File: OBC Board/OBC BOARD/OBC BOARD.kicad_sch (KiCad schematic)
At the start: 0 parts

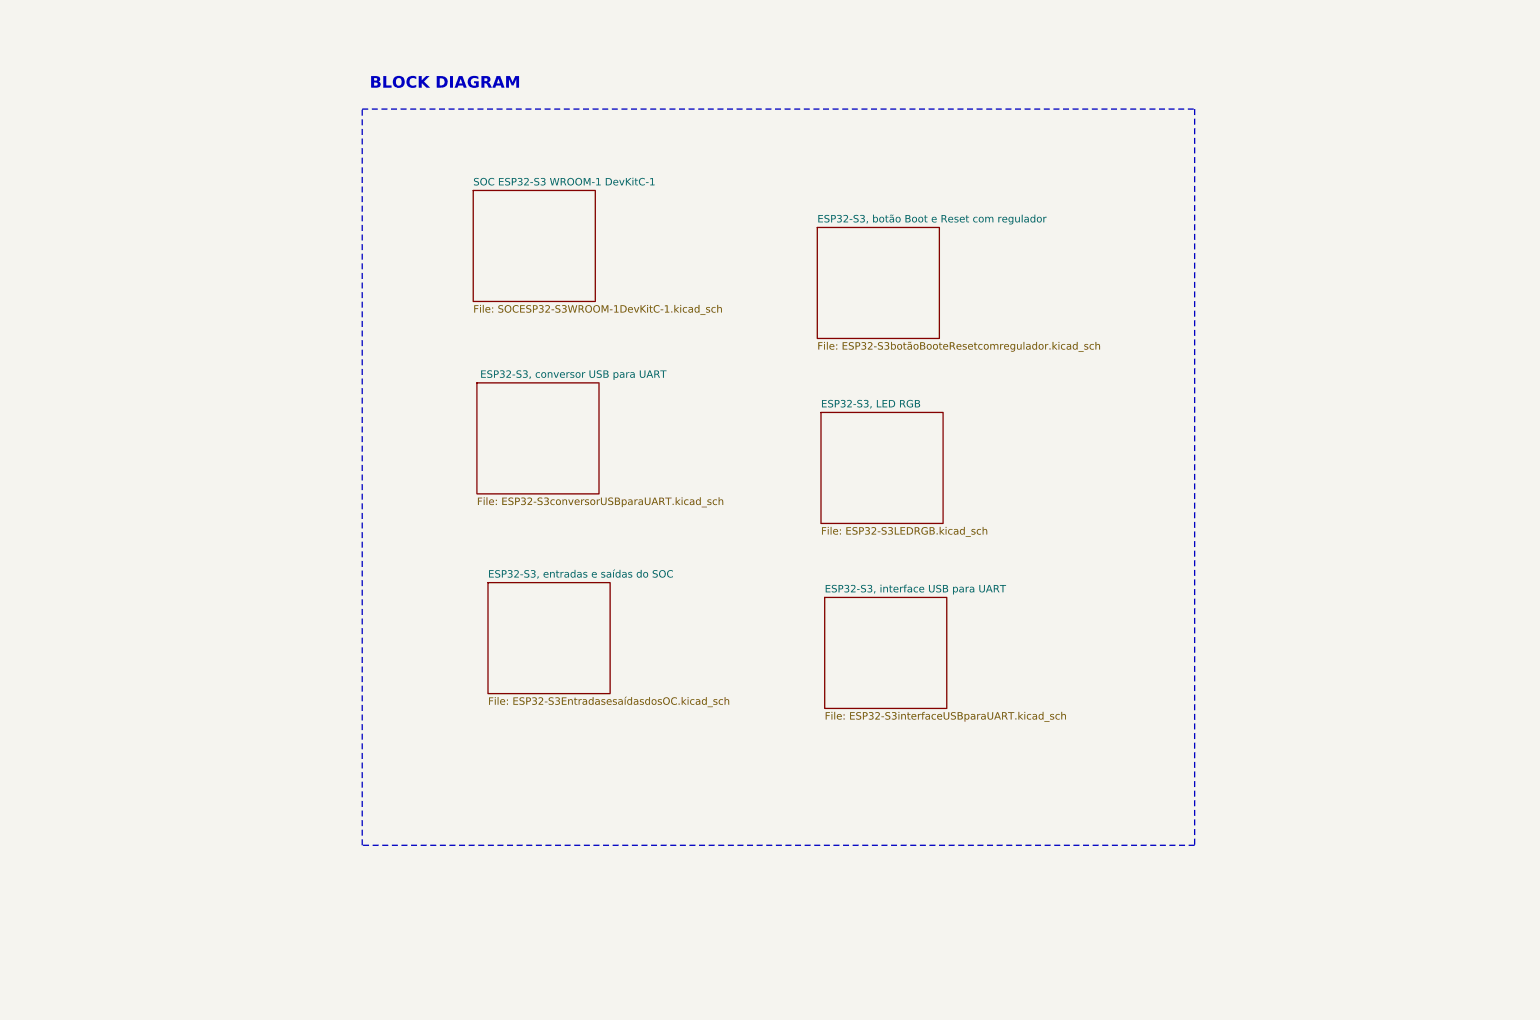
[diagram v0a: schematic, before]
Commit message: Realização do diagrama de blocos, test points, padronização e mudança dos caminhos das bibliotecas de footprints e simbolos
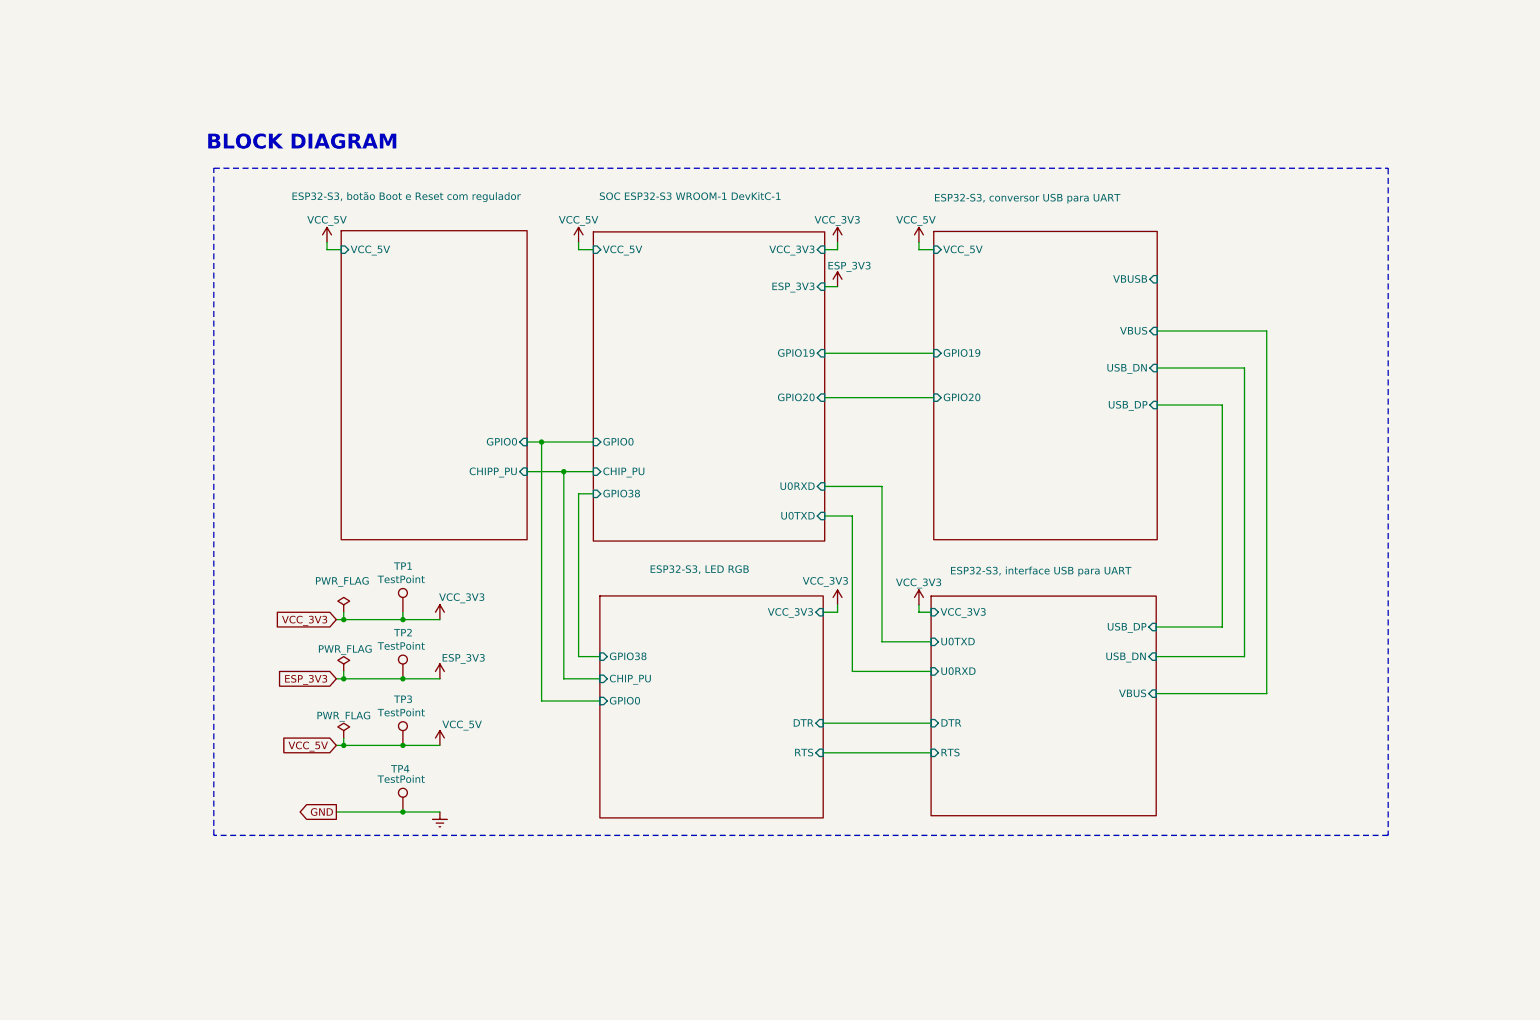
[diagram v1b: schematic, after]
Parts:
- added TP1, TP2, TP3, TP4: TestPoint, TestPoint:TestPoint_Pad_4.0x4.0mm, symbol Connector:TestPoint
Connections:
- new net ESP_3V3: TP2.1
- new net Earth: TP4.1
- new net VCC_3V3: TP1.1
- new net VCC_5V: TP3.1
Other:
- removed sheet ESP32-S3, entradas e saídas do SOC
- sheet  ESP32-S3, conversor USB para UART ports: added GPIO19, GPIO20, USB_DN, USB_DP, VBUS, VBUSB, VCC_5V; removed none
- sheet ESP32-S3, LED RGB ports: added CHIP_PU, DTR, GPIO0, GPIO38, RTS, VCC_3V3; removed none
- sheet ESP32-S3, botão Boot e Reset com regulador ports: added CHIPP_PU, GPIO0, VCC_5V; removed none
- sheet ESP32-S3, interface USB para UART ports: added DTR, RTS, U0RXD, U0TXD, USB_DN, USB_DP, VBUS, VCC_3V3; removed none
- sheet SOC ESP32-S3 WROOM-1 DevKitC-1 ports: added CHIP_PU, ESP_3V3, GPIO0, GPIO19, GPIO20, GPIO38, U0RXD, U0TXD, VCC_3V3, VCC_5V; removed none
- title: ICARUS-2 OBCH -> ICARUS-2 OBDH

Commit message: Junção dos projetos FPGA e ESP32. Biblioteca de simbolos e footprints realizadas. Definição do caminho para os arquivos. Inclusão do esquema librecube.
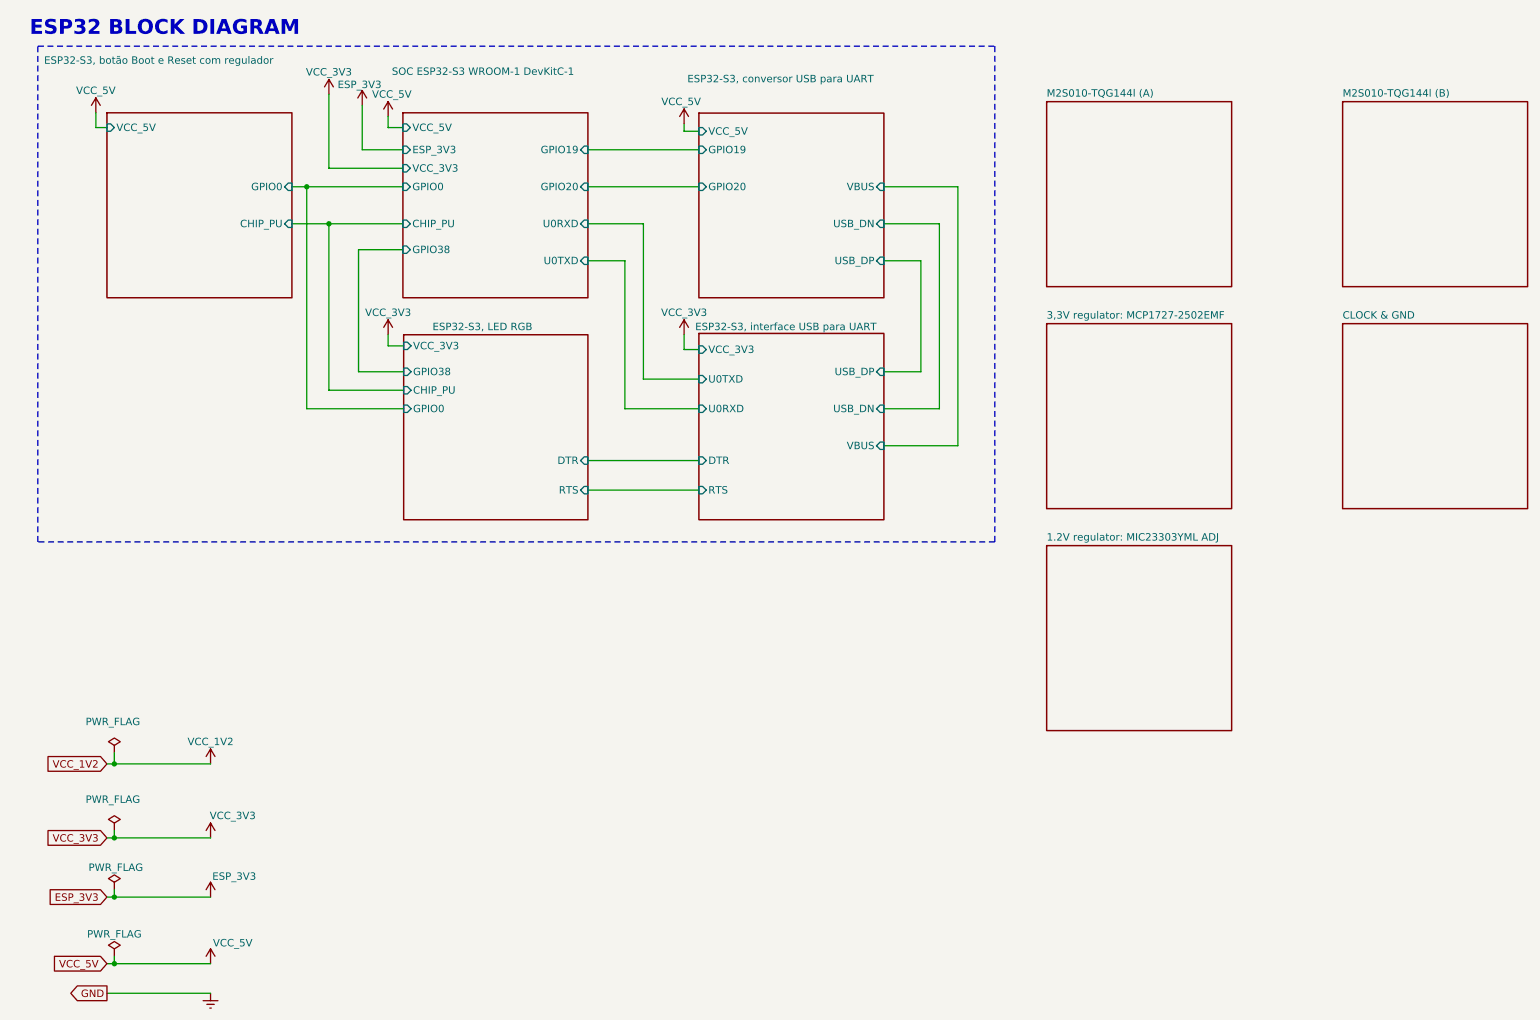
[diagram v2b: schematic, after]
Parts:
- removed TP1, TP2, TP3, TP4: TestPoint, TestPoint:TestPoint_Pad_4.0x4.0mm, symbol Connector:TestPoint
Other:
- added sheet 1.2V regulator: MIC23303YML ADJ (MIC23303YML_ADJ_1.2.kicad_sch)
- added sheet 3,3V regulator: MCP1727-2502EMF (MCP1727_2502EMF.kicad_sch)
- added sheet CLOCK & GND (CLOCK_and_GND.kicad_sch)
- added sheet M2S010-TQG144l (A) (M2S010_TQG144l_A.kicad_sch)
- added sheet M2S010-TQG144l (B) (M2S010_TQG144l_B.kicad_sch)
- sheet  ESP32-S3, conversor USB para UART ports: added none; removed VBUSB
- sheet ESP32-S3, botão Boot e Reset com regulador ports: added CHIP_PU; removed CHIPP_PU
- note added: "ESP32 BLOCK DIAGRAM"
- note removed: "BLOCK DIAGRAM"
